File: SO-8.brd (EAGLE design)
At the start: 100 x 80 mm, 3 parts

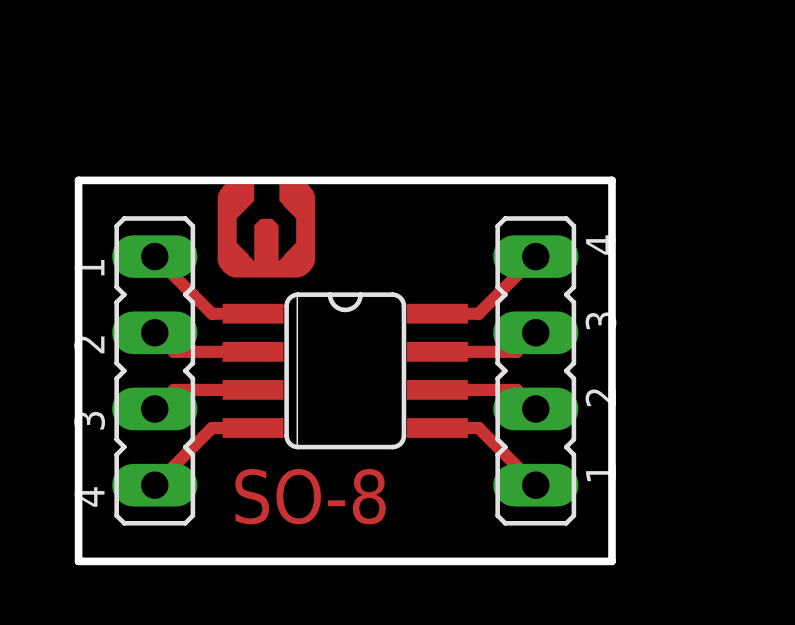
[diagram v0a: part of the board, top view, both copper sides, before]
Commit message: Increase trace clearance
The boards I made had a few shorts.
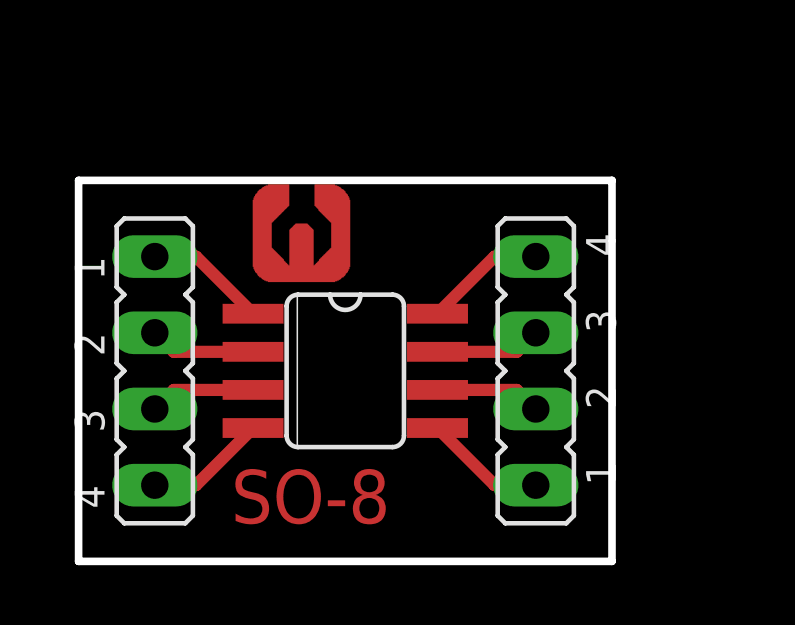
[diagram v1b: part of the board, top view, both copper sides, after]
